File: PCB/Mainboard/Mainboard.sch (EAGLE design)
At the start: 85 parts

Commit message: Redesign
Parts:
- removed BUTTON, BUTTON1, BUTTON2, BUTTON3, BUTTON4, BUTTON5: (no value), pinhead:PINHD-1X2
- removed C3, C4, C5, C6, C7: (no value), rcl:C-EUC0805
- removed JP5: (no value), pinhead:PINHD-1X6
- removed JP6: (no value), pinhead:PINHD-2X4
- removed LED10, LED11, LED12, LED3, LED4, LED5, LED6, LED7, LED8, LED9: (no value), led:LEDCHIP-LED0805
- removed LEG1, LEG2, LEG3, LEG4, LEG5, LEG6, MAIN: ATTINY1614, ATTINY1614:ATTINY1614/16/17SSNR/SSFR
- removed R10, R11, R12, R13, R14, R7, R8, R9: (no value), rcl:R-EU_R0805
- removed SERVO1, SERVO10, SERVO11, SERVO12, SERVO13, SERVO14, SERVO15, SERVO16, SERVO17, SERVO18, SERVO2, SERVO3, SERVO4, SERVO5, SERVO6, SERVO7, SERVO8, SERVO9: (no value), pinhead:PINHD-1X3
- removed SJ1, SJ10, SJ11, SJ12, SJ13, SJ14, SJ15, SJ16, SJ17, SJ18, SJ2, SJ3, SJ4, SJ5, SJ6, SJ7, SJ8, SJ9: (no value), rcl:R-EU_R0402
- removed U$2: LSF0204, LSF0204:LSF0204
- added JP1: (no value), pinhead:PINHD-1X2/90
- added LEG_0: ATTINY1614, HeRo:ATTINY1614
- added SERVO_0: SERVO_X3, HeRo:SERVO_X3
- LED1, LED2: SPICEPREFIX (none) -> L
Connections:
- removed net +3V3: U$2.VREF_B
- removed net BRK_A: MAIN.PA7, U$2.A1
- removed net BRK_B: JP5.6, U$2.B1
- removed net EN: MAIN.PA5, U$2.EN
- removed net N$1 (its old number): LEG1.PB2(TXD), R1.1
- removed net N$10: LEG1.PA6, SERVO2.1
- removed net N$11: LED3.A, R3.2
- removed net N$12: LEG1.PA7, SERVO3.1
- removed net N$13: LED4.A, R4.2
- removed net N$14: LEG2.PB2(TXD), R3.1
- removed net N$15: LEG2.PB3(RXD), R4.1
- removed net N$2 (its old number): LEG1.PB3(RXD), R2.1
- removed net N$22: LEG2.PA1(MOSI), SJ4.1
- removed net N$23: LEG2.PA2(MISO), SJ5.1
- removed net N$24: LEG2.PA3(SCK), SJ6.1
- removed net N$25: BUTTON1.1, LEG2.PA4(!SS!)
- removed net N$26: LEG2.PA5, SERVO4.1
- removed net N$27: LEG2.PA6, SERVO5.1
- removed net N$28: LEG2.PA7, SERVO6.1
- removed net N$29: LED5.A, R5.2
- removed net N$3: LEG1.PA1(MOSI), SJ1.1
- removed net N$30: LED6.A, R6.2
- removed net N$31: LEG3.PB2(TXD), R5.1
- removed net N$32: LEG3.PB3(RXD), R6.1
- removed net N$33: LEG3.PA1(MOSI), SJ7.1
- removed net N$34: LEG3.PA2(MISO), SJ8.1
- removed net N$35: LEG3.PA3(SCK), SJ9.1
- removed net N$36: BUTTON2.1, LEG3.PA4(!SS!)
- removed net N$37: LEG3.PA5, SERVO7.1
- removed net N$38: LEG3.PA6, SERVO8.1
- removed net N$39: LEG3.PA7, SERVO9.1
- removed net N$40: LED7.A, R7.2
- removed net N$41: LED8.A, R8.2
- removed net N$42: LEG4.PB2(TXD), R7.1
- removed net N$43: LEG4.PB3(RXD), R8.1
- removed net N$44: LEG4.PA1(MOSI), SJ10.1
- removed net N$45: LEG4.PA2(MISO), SJ11.1
- removed net N$46: LEG4.PA3(SCK), SJ12.1
- removed net N$47: BUTTON3.1, LEG4.PA4(!SS!)
- removed net N$48: LEG4.PA5, SERVO10.1
- removed net N$49: LEG4.PA6, SERVO11.1
- removed net N$5: LEG1.PA3(SCK), SJ3.1
- removed net N$50: LEG4.PA7, SERVO12.1
- removed net N$51: LED9.A, R9.2
- removed net N$52: LED10.A, R10.2
- removed net N$53: LEG5.PB2(TXD), R9.1
- removed net N$54: LEG5.PB3(RXD), R10.1
- removed net N$55: LEG5.PA1(MOSI), SJ13.1
- removed net N$56: LEG5.PA2(MISO), SJ14.1
- removed net N$57: LEG5.PA3(SCK), SJ15.1
- removed net N$58: BUTTON4.1, LEG5.PA4(!SS!)
- removed net N$59: LEG5.PA5, SERVO13.1
- removed net N$60: LEG5.PA6, SERVO14.1
- removed net N$61: LEG5.PA7, SERVO15.1
- removed net N$62: LED11.A, R11.2
- removed net N$63: LED12.A, R12.2
- removed net N$64: LEG6.PB2(TXD), R11.1
- removed net N$65: LEG6.PB3(RXD), R12.1
- removed net N$66: LEG6.PA1(MOSI), SJ16.1
- removed net N$67: LEG6.PA2(MISO), SJ17.1
- removed net N$68: LEG6.PA3(SCK), SJ18.1
- removed net N$69: BUTTON5.1, LEG6.PA4(!SS!)
- removed net N$70: LEG6.PA5, SERVO16.1
- removed net N$71: LEG6.PA6, SERVO17.1
- removed net N$72: LEG6.PA7, SERVO18.1
- removed net N$8: BUTTON.1, LEG1.PA4(!SS!)
- removed net N$9: LEG1.PA5, SERVO1.1
- removed net RXD_A: MAIN.PB3(RXD), U$2.A3
- removed net RXD_B: JP5.5, U$2.B2
- removed net STATE_A: MAIN.PA6, U$2.A4
- removed net STATE_B: JP5.1, U$2.B4
- removed net TXD_A: MAIN.PB2(TXD), U$2.A2
- removed net TXD_B: JP5.4, U$2.B3
- removed net UPDI0: JP6.6, MAIN.PA0(!RST!/UPDI/A0)
- removed net UPDI1: JP6.5, LEG1.PA0(!RST!/UPDI/A0)
- removed net UPDI2: JP6.8, LEG2.PA0(!RST!/UPDI/A0)
- removed net UPDI3: JP6.7, LEG3.PA0(!RST!/UPDI/A0)
- removed net UPDI4: JP6.4, LEG4.PA0(!RST!/UPDI/A0)
- removed net UPDI5: JP6.3, LEG5.PA0(!RST!/UPDI/A0)
- removed net UPDI6: JP6.1, LEG6.PA0(!RST!/UPDI/A0)
- removed net VCC: SERVO1.2, SERVO2.2, SERVO3.2, SERVO4.2, SERVO5.2, SERVO6.2, SERVO7.2, SERVO8.2, SERVO9.2
- removed net VCC/2: SERVO10.2, SERVO11.2, SERVO12.2, SERVO13.2, SERVO14.2, SERVO15.2, SERVO16.2, SERVO17.2, SERVO18.2
- new net ADDA_0: LEG_0.PA7, R3.1
- new net ADDB_0: LEG_0.PA6, R4.1
- new net ADDC_0: LEG_0.PA5, R5.1
- new net LEDA_0: LEG_0.PA4, R1.1
- new net LEDB_0: LEG_0.PA3, R2.1
- new net PWMA_0: LEG_0.PB0, SERVO_0.PWMA
- new net PWMB_0: LEG_0.PB1, SERVO_0.PWMB
- new net PWMC_0: LEG_0.PB2, SERVO_0.PWMC
- new net SENSE_0: C2.1, LEG_0.PB3, R6.1
- new net UPDI_0: LEG_0.PA0
- new net VDD: SERVO_0.VCC
- net +5V: now also LEG_0.VCC; no longer C2.1, C3.1, C4.1, C5.1, C6.1, C7.1, JP5.2, LEG1.VCC, LEG2.VCC, LEG3.VCC, LEG4.VCC, LEG5.VCC, LEG6.VCC, MAIN.VCC, R13.2, R14.2, U$2.VREF_A
- net GND: now also JP1.2, LEG_0.GND, R3.2, R4.2, R5.2, SERVO_0.GND; no longer BUTTON.2, BUTTON1.2, BUTTON2.2, BUTTON3.2, BUTTON4.2, BUTTON5.2, C3.2, C4.2, C5.2, C6.2, C7.2, JP5.3, JP6.2, LED10.C, LED11.C, LED12.C, LED3.C, LED4.C, LED5.C, LED6.C, LED7.C, LED8.C, LED9.C, LEG1.GND, LEG2.GND, LEG3.GND, LEG4.GND, LEG5.GND, LEG6.GND, MAIN.GND, SERVO1.3, SERVO10.3, SERVO11.3, SERVO12.3, SERVO13.3, SERVO14.3, SERVO15.3, SERVO16.3, SERVO17.3, SERVO18.3, SERVO2.3, SERVO3.3, SERVO4.3, SERVO5.3, SERVO6.3, SERVO7.3, SERVO8.3, SERVO9.3, SJ1.2, SJ10.2, SJ11.2, SJ12.2, SJ13.2, SJ14.2, SJ15.2, SJ16.2, SJ17.2, SJ18.2, SJ2.2, SJ3.2, SJ4.2, SJ5.2, SJ6.2, SJ7.2, SJ8.2, SJ9.2, U$2.GND
- net N$4: now also JP1.1, R6.2; no longer LEG1.PA2(MISO), SJ2.1
- net SCL: now also LEG_0.PA2; no longer LEG1.PB0(SCL), LEG2.PB0(SCL), LEG3.PB0(SCL), LEG4.PB0(SCL), LEG5.PB0(SCL), LEG6.PB0(SCL), MAIN.PB0(SCL), R14.1
- net SDA: now also LEG_0.PA1; no longer LEG1.PB1(SDA), LEG2.PB1(SDA), LEG3.PB1(SDA), LEG4.PB1(SDA), LEG5.PB1(SDA), LEG6.PB1(SDA), MAIN.PB1(SDA), R13.1
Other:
- note removed: "TODO: Sensor I2C-Port 3.3V Regler 5V Regler? Power-Verbinder Led? Buttoncon?"

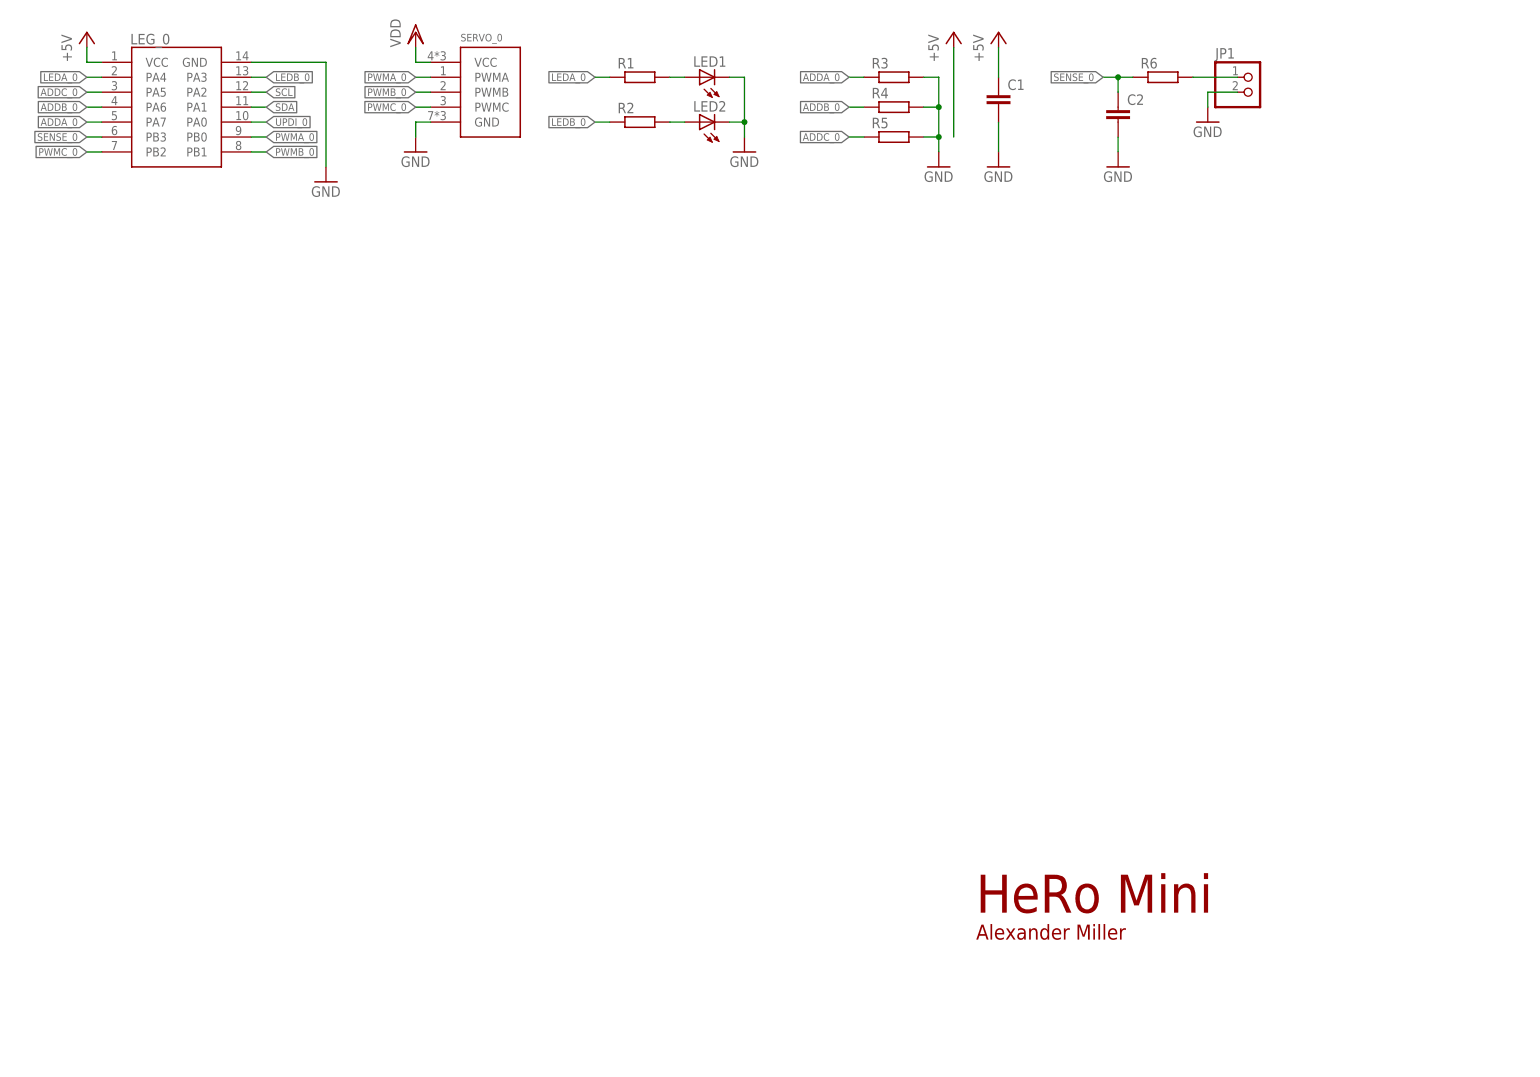
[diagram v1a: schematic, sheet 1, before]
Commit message: Finished Servocontroller design
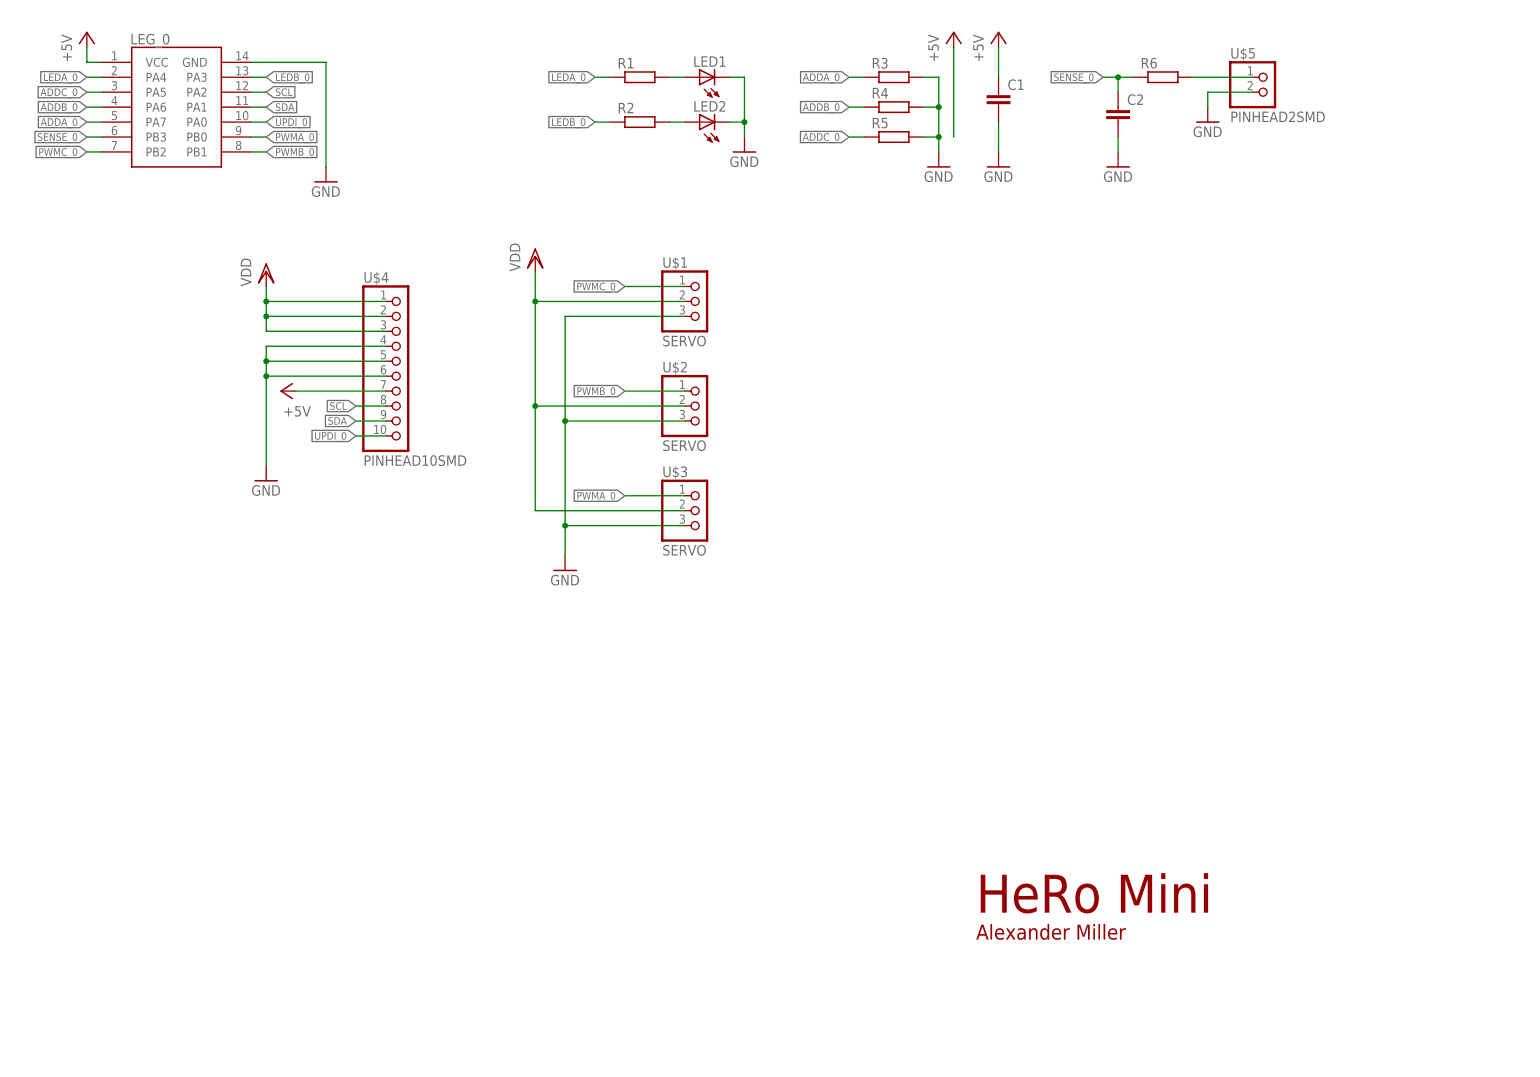
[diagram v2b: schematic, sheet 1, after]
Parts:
- removed JP1: (no value), pinhead:PINHD-1X2/90
- removed SERVO_0: SERVO_X3, HeRo:SERVO_X3
- added U$1, U$2, U$3: SERVO, HeRo:SERVO
- added U$4: PINHEAD10SMD, HeRo:PINHEAD10SMD
- added U$5: PINHEAD2SMD, HeRo:PINHEAD2SMD
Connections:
- net +5V: now also U$4.7
- net GND: now also U$1.3, U$2.3, U$3.3, U$4.4, U$4.5, U$4.6, U$5.2; no longer JP1.2, SERVO_0.GND
- net N$4: now also U$5.1; no longer JP1.1
- net PWMA_0: now also U$3.1; no longer SERVO_0.PWMA
- net PWMB_0: now also U$2.1; no longer SERVO_0.PWMB
- net PWMC_0: now also U$1.1; no longer SERVO_0.PWMC
- net SCL: now also U$4.8
- net SDA: now also U$4.9
- net UPDI_0: now also U$4.10
- net VDD: now also U$1.2, U$2.2, U$3.2, U$4.1, U$4.2, U$4.3; no longer SERVO_0.VCC

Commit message: Minor changes in controller, new mainboard
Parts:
- removed C1, C2: (no value), rcl:C-EUC0805
- removed LED1, LED2: (no value), led:LEDCHIP-LED0805
- removed LEG_0: ATTINY1614, HeRo:ATTINY1614
- removed R1, R2, R3, R4, R5, R6: (no value), rcl:R-EU_R0805
- removed U$2, U$3: SERVO, HeRo:SERVO
- removed U$4: PINHEAD10SMD, HeRo:PINHEAD10SMD
- removed U$5: PINHEAD2SMD, HeRo:PINHEAD2SMD
- added LEG0, LEG1, LEG2, LEG3, LEG4, LEG5: (no value), pinhead:PINHD-1X10
- U$1: value SERVO -> ESP32-DOITV1; device HeRo:SERVO -> HeRo:ESP32-DOITV1
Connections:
- removed net ADDA_0: LEG_0.PA7, R3.1
- removed net ADDB_0: LEG_0.PA6, R4.1
- removed net ADDC_0: LEG_0.PA5, R5.1
- removed net LEDA_0: LEG_0.PA4, R1.1
- removed net LEDB_0: LEG_0.PA3, R2.1
- removed net N$1: LED1.A, R1.2
- removed net N$2: LED2.A, R2.2
- removed net N$4: R6.2, U$5.1
- removed net PWMA_0: LEG_0.PB0, U$3.1
- removed net PWMB_0: LEG_0.PB1, U$2.1
- removed net PWMC_0: LEG_0.PB2, U$1.1
- removed net SENSE_0: C2.1, LEG_0.PB3, R6.1
- new net UPDI_1: LEG1.10
- new net UPDI_2: LEG2.10
- new net UPDI_3: LEG3.10
- new net UPDI_4: LEG4.10
- new net UPDI_5: LEG5.10
- net +5V: now also LEG0.7, LEG1.7, LEG2.7, LEG3.7, LEG4.7, LEG5.7; no longer C1.1, LEG_0.VCC, U$4.7
- net GND: now also LEG0.4, LEG0.5, LEG0.6, LEG1.4, LEG1.5, LEG1.6, LEG2.4, LEG2.5, LEG2.6, LEG3.4, LEG3.5, LEG3.6, LEG4.4, LEG4.5, LEG4.6, LEG5.4, LEG5.5, LEG5.6; no longer C1.2, C2.2, LED1.C, LED2.C, LEG_0.GND, R3.2, R4.2, R5.2, U$1.3, U$2.3, U$3.3, U$4.4, U$4.5, U$4.6, U$5.2
- net SCL: now also LEG0.8, LEG1.8, LEG2.8, LEG3.8, LEG4.8, LEG5.8, U$1.IO22; no longer LEG_0.PA2, U$4.8
- net SDA: now also LEG0.9, LEG1.9, LEG2.9, LEG3.9, LEG4.9, LEG5.9, U$1.IO21; no longer LEG_0.PA1, U$4.9
- net UPDI_0: now also LEG0.10; no longer LEG_0.PA0, U$4.10
- net VDD: now also LEG0.1, LEG0.2, LEG0.3, LEG1.1, LEG1.2, LEG1.3, LEG2.1, LEG2.2, LEG2.3, LEG3.1, LEG3.2, LEG3.3, LEG4.1, LEG4.2, LEG4.3, LEG5.1, LEG5.2, LEG5.3; no longer U$1.2, U$2.2, U$3.2, U$4.1, U$4.2, U$4.3

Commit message: WIP Mainboard design
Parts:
- added I2C-PWR-SELECT: (no value), pinhead:PINHD-1X3
- added JP1, JP2: (no value), pinhead:PINHD-1X18
- added PWR-SELECT: (no value), pinhead:PINHD-2X3
- added R1, R2: 10k, rcl:R-EU_R0805
- added U$2: D24V150F6, HeRo:D24V150F6
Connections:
- removed net UPDI_0: LEG0.10
- removed net UPDI_1: LEG1.10
- removed net UPDI_2: LEG2.10
- removed net UPDI_3: LEG3.10
- removed net UPDI_4: LEG4.10
- removed net UPDI_5: LEG5.10
- new net 3V3-1: I2C-PWR-SELECT.1, JP1.15, U$1.3V3
- new net 3V3-2: I2C-PWR-SELECT.3, JP1.18, U$1.CLK
- new net GND1: JP2.14, PWR-SELECT.2, U$1.GND
- new net GND2: JP2.17, PWR-SELECT.6, U$1.SD3
- new net N$1: I2C-PWR-SELECT.2, R1.2, R2.2
- new net N$10: JP2.9, U$1.D26
- new net N$11: JP2.10, U$1.D27
- new net N$12: JP2.11, U$1.D14
- new net N$13: JP2.12, U$1.D12
- new net N$14: JP2.13, U$1.D13
- new net N$15: JP2.16, U$1.SD2
- new net N$16: JP1.17, U$1.SD0
- new net N$17: JP1.16, U$1.SD1
- new net N$18: JP1.14, U$1.D0
- new net N$19: JP1.13, U$1.D15
- new net N$2: JP2.1, U$1.EN
- new net N$20: JP1.12, U$1.D2
- new net N$21: JP1.11, U$1.D4
- new net N$22: JP1.10, U$1.RX2
- new net N$23: JP1.9, U$1.TX2
- new net N$24: JP1.8, U$1.D5
- new net N$25: JP1.7, U$1.D18
- new net N$26: JP1.6, U$1.D19
- new net N$27: JP1.4, U$1.RX0
- new net N$28: JP1.3, U$1.TX0
- new net N$29: JP1.1, U$1.D23
- new net N$3: JP2.2, U$1.VP
- new net N$4: JP2.3, U$1.VN
- new net N$5: JP2.4, U$1.D34
- new net N$6: JP2.5, U$1.D35
- new net N$7: JP2.6, U$1.D32
- new net N$8: JP2.7, U$1.D33
- new net N$9: JP2.8, U$1.D25
- new net VCC1: JP2.15, PWR-SELECT.1, U$1.VIN
- new net VCC2: JP2.18, PWR-SELECT.5, U$1.CMD
- net +5V: now also LEG0.4, LEG1.4, LEG2.4, LEG3.4, LEG4.4, LEG5.4, PWR-SELECT.3; no longer LEG0.7, LEG1.7, LEG2.7, LEG3.7, LEG4.7, LEG5.7
- net GND: now also LEG0.10, LEG0.8, LEG0.9, LEG1.10, LEG1.8, LEG1.9, LEG2.10, LEG2.8, LEG2.9, LEG3.10, LEG3.8, LEG3.9, LEG4.10, LEG4.8, LEG4.9, LEG5.10, LEG5.8, LEG5.9, PWR-SELECT.4; no longer LEG0.4, LEG0.5, LEG0.6, LEG1.4, LEG1.5, LEG1.6, LEG2.4, LEG2.5, LEG2.6, LEG3.4, LEG3.5, LEG3.6, LEG4.4, LEG4.5, LEG4.6, LEG5.4, LEG5.5, LEG5.6
- net SCL: now also JP1.2, LEG0.5, LEG1.5, LEG2.5, LEG3.5, LEG4.5, LEG5.5, R2.1, U$1.D22; no longer LEG0.8, LEG1.8, LEG2.8, LEG3.8, LEG4.8, LEG5.8, U$1.IO22
- net SDA: now also JP1.5, LEG0.6, LEG1.6, LEG2.6, LEG3.6, LEG4.6, LEG5.6, R1.1, U$1.D21; no longer LEG0.9, LEG1.9, LEG2.9, LEG3.9, LEG4.9, LEG5.9, U$1.IO21
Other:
- moved on the sheet: LEG0, LEG1, LEG2, LEG3, LEG4, LEG5

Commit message: Minor Changes
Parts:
- added U$3: GY-521_MPU6050, HeRo:GY-521_MPU6050
- added U$4: VL53L0XV, HeRo:VL53L0XV
- added U$5: D24V10F5, HeRo:D24V10F5
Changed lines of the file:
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@@
 <?xml version="1.0" encoding="utf-8"?>
 <!DOCTYPE eagle SYSTEM "eagle.dtd">
-<eagle version="9.0.0">
+<eagle version="8.7.0">
 <drawing>
 <settings>
@@
 </part>
 <part name="U$2" library="HeRo" deviceset="D24V150F6" device=""/>
+<part name="U$3" library="HeRo" deviceset="GY-521_MPU6050" device=""/>
+<part name="U$4" library="HeRo" deviceset="VL53L0X" device="V"/>
+<part name="U$5" library="HeRo" deviceset="D24V10F5" device=""/>
 </parts>
 <sheets>
@@
 <instance part="VDD6" gate="G$1" x="83.82" y="116.84"/>
 <instance part="U$2" gate="G$1" x="50.8" y="48.26"/>
+<instance part="U$3" gate="G$1" x="101.6" y="50.8"/>
+<instance part="U$4" gate="G$1" x="144.78" y="48.26"/>
+<instance part="U$5" gate="G$1" x="167.64" y="53.34"/>
 </instances>
 <busses>

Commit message: Minor Redesign
Replace ESP32 Eval board with own design
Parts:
- removed I2C-PWR-SELECT: (no value), pinhead:PINHD-1X3
- removed JP1, JP2: (no value), pinhead:PINHD-1X18
- removed LEG0: (no value), pinhead:PINHD-1X10
- removed PWR-SELECT: (no value), pinhead:PINHD-2X3
- removed U$2: D24V150F6, HeRo:D24V150F6
- removed U$5: D24V10F5, HeRo:D24V10F5
- added C1, C2: 100nF, rcl:C-EUC0805
- added IC1: FT232RL, ftdichip:FT232RL
- added J1: (no value), InputOutputIO (rev18a):629105136821
- added LED1, LED2: (no value), led:LEDCHIP-LED0805
- added LEG6: (no value), pinhead:PINHD-1X10
- added PWR_INPUT, PWR_SERVO_IN, PWR_SERVO_OUT: CON-PHOENIX-1935310, HeRo:CON-PHOENIX-1935310
- added R3, R4: 10k, rcl:R-EU_R0805
- added R5, R6: (no value), rcl:R-EU_R0805
- added U$100: ESP32-DOITV1, HeRo:ESP32-DOITV1
- U$1: value ESP32-DOITV1 -> VL53L0XV; device HeRo:ESP32-DOITV1 -> HeRo:VL53L0XV
- U$3: value GY-521_MPU6050 -> D24V10F5; device HeRo:GY-521_MPU6050 -> HeRo:D24V10F5
- U$4: value VL53L0XV -> D24V150F6; device HeRo:VL53L0XV -> HeRo:D24V150F6
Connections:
- removed net 3V3-1: I2C-PWR-SELECT.1, JP1.15, U$1.3V3
- removed net 3V3-2: I2C-PWR-SELECT.3, JP1.18, U$1.CLK
- removed net GND1: JP2.14, PWR-SELECT.2, U$1.GND
- removed net GND2: JP2.17, PWR-SELECT.6, U$1.SD3
- removed net N$10: JP2.9, U$1.D26
- removed net N$11: JP2.10, U$1.D27
- removed net N$12: JP2.11, U$1.D14
- removed net N$13: JP2.12, U$1.D12
- removed net N$14: JP2.13, U$1.D13
- removed net N$15: JP2.16, U$1.SD2
- removed net N$16: JP1.17, U$1.SD0
- removed net N$17: JP1.16, U$1.SD1
- removed net N$18: JP1.14, U$1.D0
- removed net N$19: JP1.13, U$1.D15
- removed net N$20: JP1.12, U$1.D2
- removed net N$21: JP1.11, U$1.D4
- removed net N$22: JP1.10, U$1.RX2
- removed net N$23: JP1.9, U$1.TX2
- removed net N$24: JP1.8, U$1.D5
- removed net N$25: JP1.7, U$1.D18
- removed net N$26: JP1.6, U$1.D19
- removed net N$27: JP1.4, U$1.RX0
- removed net N$28: JP1.3, U$1.TX0
- removed net N$29: JP1.1, U$1.D23
- removed net N$8: JP2.7, U$1.D33
- removed net N$9: JP2.8, U$1.D25
- removed net VCC1: JP2.15, PWR-SELECT.1, U$1.VIN
- removed net VCC2: JP2.18, PWR-SELECT.5, U$1.CMD
- new net !CTS: IC1.!CTS
- new net !DTR: IC1.!DTR
- new net !RTS: IC1.!RTS
- new net +12V: PWR_INPUT.1, PWR_SERVO_IN.1, U$3.VIN, U$4.VIN
- new net +3V3: R2.1, R3.1
- new net EN_5V: U$3.!SHDN
- new net EN_SERVO: U$4.EN
- new net PG_LEG: R3.2, U$3.PG
- new net PG_SERVO: R2.2, U$4.PG
- new net RXD: IC1.RXD
- new net SCL_5V: U$1.SCL
- new net SDA_5V: U$1.SDA
- new net TXD: IC1.TXD
- new net USB_D_N: IC1.USBDM, J1.D-
- new net USB_D_P: IC1.USBDP, J1.D+
- new net VBUS: C2.1, IC1.VCC, J1.VBUS
- net +5V: now also LEG6.4, U$1.VIN, U$3.VOUT; no longer LEG0.4, PWR-SELECT.3
- net GND: now also C1.2, C2.2, IC1.GND, IC1.GND@1, IC1.GND@2, IC1.GND@A, IC1.TEST, J1.GND, LEG6.10, LEG6.8, LEG6.9, PWR_INPUT.2, PWR_SERVO_IN.2, PWR_SERVO_OUT.1, R1.1, U$1.GND, U$3.GND, U$4.GND; no longer LEG0.10, LEG0.8, LEG0.9, PWR-SELECT.4
- net N$1: now also C1.1, IC1.3V3OUT, IC1.VCCIO, R4.1, R5.2, R6.2; no longer I2C-PWR-SELECT.2, R1.2, R2.2
- net N$2: now also R1.2, U$4.MOD; no longer JP2.1, U$1.EN
- net N$3: now also IC1.!RESET, R4.2; no longer JP2.2, U$1.VP
- net N$4: now also IC1.CBUS0, LED1.C; no longer JP2.3, U$1.VN
- net N$5: now also IC1.CBUS1, LED2.C; no longer JP2.4, U$1.D34
- net N$6: now also LED1.A, R5.1; no longer JP2.5, U$1.D35
- net N$7: now also LED2.A, R6.1; no longer JP2.6, U$1.D32
- net SCL: now also LEG6.5; no longer JP1.2, LEG0.5, R2.1, U$1.D22
- net SDA: now also LEG6.6; no longer JP1.5, LEG0.6, R1.1, U$1.D21
- net VDD: now also LEG6.1, LEG6.2, LEG6.3, PWR_SERVO_OUT.2, U$4.VOUT; no longer LEG0.1, LEG0.2, LEG0.3
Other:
- note added: "!SHDN! high=on, PU VIN"
- note added: "EN >2V=ON, PU=5V"
- note added: "ESP32"
- note added: "Leg Controller"
- note added: "MOD intern PD"
- note added: "PG PU Needed"
- note added: "Power"
- note added: "Sensor"
- note added: "VIN 4V-36V"
- note added: "VIN 8-40V"
- note added: "VOUT 5V 1A"
- note added: "VOUT 6V 15A"
